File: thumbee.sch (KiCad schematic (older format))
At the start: 1 part, among them U1 msc313e

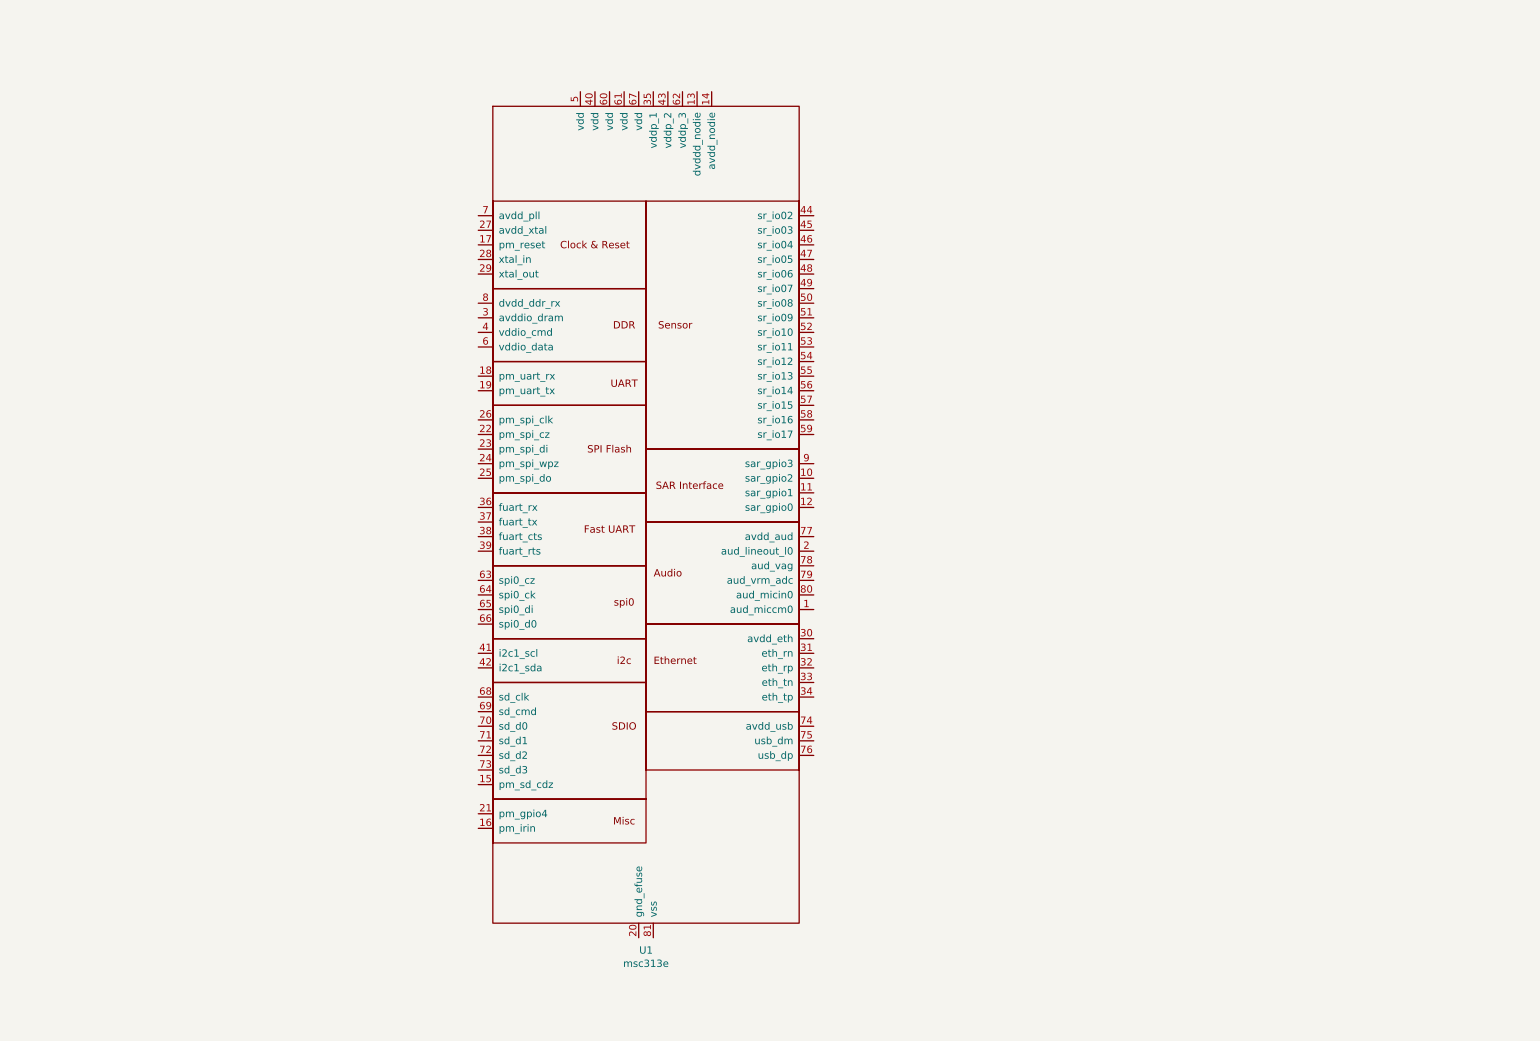
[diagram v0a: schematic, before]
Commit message: Add remaining required components. Clean up schematic a bit.
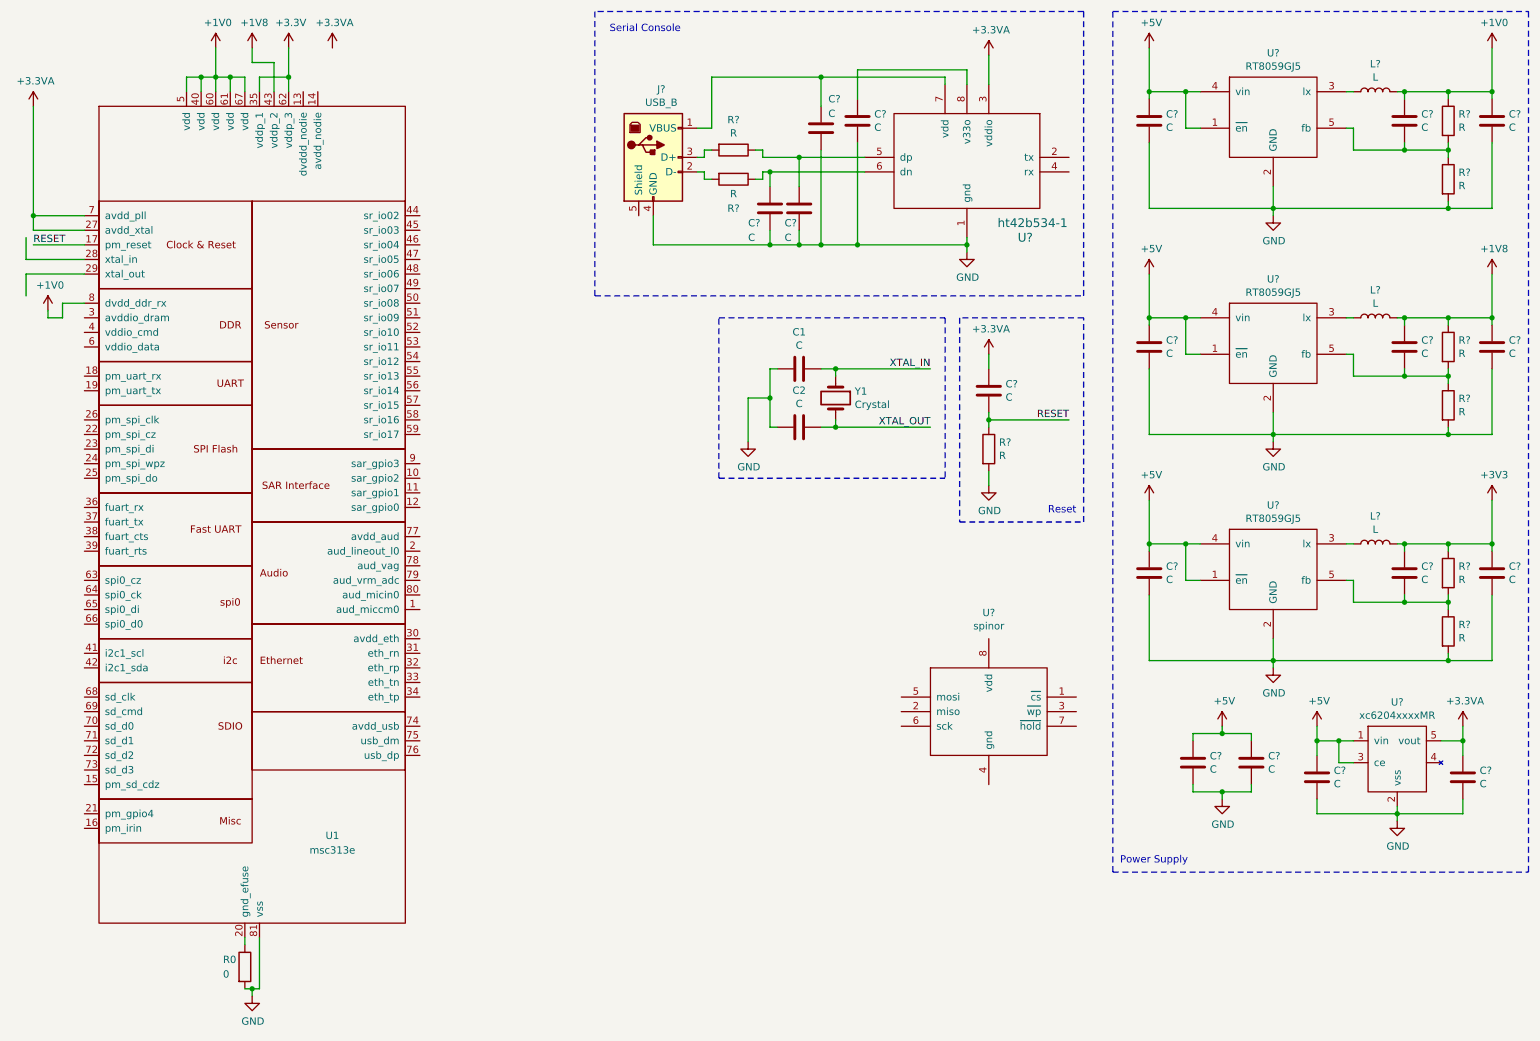
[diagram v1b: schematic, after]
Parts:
- added C1, C2, C? (x18): C, symbol Device:C
- added J?: USB_B, symbol Connector:USB_B
- added L? (x3): L, symbol Device:L
- added R0: 0, symbol Device:R
- added R? (x9): R, symbol Device:R
- added U?: ht42b534-1, symbol ht42b534-1:ht42b534-1
- added U? (x3): RT8059GJ5, symbol rt8059gj5:RT8059GJ5
- added U?: spinor, symbol spinor:spinor
- added U?: xc6204xxxxMR, symbol xc6204:xc6204xxxxMR
- added Y1: Crystal, symbol Device:Crystal
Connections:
- net RESET: now reaches U1.17 (pm_reset)
- net RESET: now also C?.2, R?.1
- net at U1.20 (gnd_efuse): now also R0.1
- net +3.3VA: now reaches U1.27 (avdd_xtal)
- net +3.3VA: now also U1.7 (avdd_pll), C?.1, C?.1, U?.3 (vddio), U?.5 (vout)
- net +3V3: now reaches U1.35 (vddp_1)
- net +3V3: now also U1.62 (vddp_3), C?.1, C?.1, L?.2, R?.1
- net +1V0: now reaches U1.40 (vdd)
- net +1V0: now also U1.5 (vdd), U1.60 (vdd), U1.61 (vdd), U1.67 (vdd), U1.8 (dvdd_ddr_rx), C?.1, C?.1, L?.2, R?.1
- net +1V8: now reaches U1.43 (vddp_2)
- net +1V8: now also C?.1, C?.1, L?.2, R?.1
- net GND: now reaches U1.81 (vss)
- net GND: now also C1.2, C2.1, C?.2, C?.2, C?.2, C?.2, C?.2, C?.2, C?.2, C?.2, C?.2, C?.2, C?.2, C?.2, C?.2, C?.2, J?.4 (GND), R0.2, R?.2, R?.2, R?.2, R?.2, U?.1 (gnd), U?.2 (GND), U?.2 (GND), U?.2 (GND), U?.2 (vss)
- new net: C?.1, R?.1, U?.5 (dp)
- new net: C?.1, R?.1, U?.6 (dn)
- new net: C?.1, J?.1 (VBUS), U?.7 (vdd)
- new net: C?.1, U?.8 (v33o)
- new net: L?.1, U?.3 (lx) (x3)
- new net: C?.2, R?.1, R?.2, U?.5 (fb) (x3)
- new net: J?.2 (D-), R?.2
- new net: J?.3 (D+), R?.2
- new net +5V: C?.1, C?.1, C?.1, C?.1, C?.1, C?.1, U?.1 (vin), U?.1 (~en), U?.1 (~en), U?.1 (~en), U?.3 (ce), U?.4 (vin), U?.4 (vin), U?.4 (vin)
- new net XTAL_IN: C1.1, Y1.1
- new net XTAL_OUT: C2.2, Y1.2
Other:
- note added: "Power Supply"
- note added: "Reset"
- note added: "Serial Console"
- moved on the sheet: U1

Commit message: Almost complete schematic
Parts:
- added C? (x6): C, symbol Device:C
- added J10, J11, J4: Conn_01x02_Male, symbol Connector:Conn_01x02_Male
- added J12: Conn_02x05_Odd_Even, symbol Connector_Generic:Conn_02x05_Odd_Even
- added J2, J3, J7, J9: Conn_01x04_Male, symbol Connector:Conn_01x04_Male
- added J5: Conn_01x07_Male, symbol Connector:Conn_01x07_Male
- added J6: Conn_01x16_Male, symbol Connector:Conn_01x16_Male
- added J8: Conn_01x05_Male, symbol Connector:Conn_01x05_Male
- added R10, R2, R3, R5, R6, R7, R8, R9, R?: R, symbol Device:R
- gave numbers to parts that had none: 12
- renumbered R0 to R1
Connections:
- net XTAL_OUT is gone; now on net xtal_out: C2.2, Y1.2
- net +1V8: now also U1.3 (avddio_dram), U1.4 (vddio_cmd), U1.6 (vddio_data), C?.1, C?.1, C?.1, R10.1, R5.1, R7.1, R8.1, R9.1, R?.1; no longer U1.43 (vddp_2)
- net +3.3VA: now also U1.14 (avdd_nodie), U1.30 (avdd_eth), U1.74 (avdd_usb), U1.77 (avdd_aud)
- net +3V3: now also U2.8 (vdd), C?.1, J12.1 (Pin_1), R6.1; no longer U1.35 (vddp_1), U1.62 (vddp_3)
- net +5V: no longer U7.1 (~en)
- net GND: now also U2.4 (gnd), C?.1, C?.2, C?.2, C?.2, C?.2, C?.2, J12.10 (Pin_10)
- net at U1.1 (aud_miccm0): now also J8.5 (Pin_5)
- net at U1.10 (sar_gpio2): now also J7.2 (Pin_2)
- net at U1.11 (sar_gpio1): now also J7.3 (Pin_3)
- net at U1.12 (sar_gpio0): now also J7.4 (Pin_4)
- net dvdd_nodie: now reaches U1.13 (dvddd_nodie)
- net dvdd_nodie: now also C?.2
- net at U1.15 (pm_sd_cdz): now also J5.7 (Pin_7)
- net console_tx: now reaches U1.18 (pm_uart_rx)
- net console_tx: now also U3.2 (tx)
- net console_rx: now reaches U1.19 (pm_uart_tx)
- net console_rx: now also U3.4 (rx)
- net at U1.2 (aud_lineout_l0): now also J8.1 (Pin_1)
- net gnd_efuse: now reaches R1.1, U1.20 (gnd_efuse)
- net at U1.21 (pm_gpio4): now also J11.1 (Pin_1)
- net spinor_cs: now reaches U1.22 (pm_spi_cz)
- net spinor_cs: now also U2.1 (~cs), J12.2 (Pin_2)
- net spinor_miso: now reaches U1.23 (pm_spi_di)
- net spinor_miso: now also U2.2 (miso), J12.5 (Pin_5)
- net spinor_wp: now reaches U1.24 (pm_spi_wpz)
- net spinor_wp: now also U2.3 (~wp), J12.4 (Pin_4)
- net spinor_mosi: now reaches U1.25 (pm_spi_do)
- net spinor_mosi: now also U2.5 (mosi), J12.3 (Pin_3)
- net spinor_clk: now reaches U1.26 (pm_spi_clk)
- net xtal_in: now reaches U1.28 (xtal_in)
- net xtal_in: now also R2.1
- net xtal_out: now reaches U1.29 (xtal_out)
- net xtal_out: now also R3.2
- net at U1.31 (eth_rn): now also J9.1 (Pin_1)
- net at U1.32 (eth_rp): now also J9.2 (Pin_2)
- net at U1.33 (eth_tn): now also J9.3 (Pin_3)
- net at U1.34 (eth_tp): now also J9.4 (Pin_4)
- net at U1.36 (fuart_rx): now also J2.1 (Pin_1)
- net at U1.37 (fuart_tx): now also J2.2 (Pin_2)
- net at U1.38 (fuart_cts): now also J2.3 (Pin_3)
- net at U1.39 (fuart_rts): now also J2.4 (Pin_4)
- net at U1.41 (i2c1_scl): now also J4.1 (Pin_1)
- net at U1.42 (i2c1_sda): now also J4.2 (Pin_2)
- net at U1.44 (sr_io02): now also J6.1 (Pin_1)
- net at U1.45 (sr_io03): now also J6.2 (Pin_2)
- net at U1.46 (sr_io04): now also J6.3 (Pin_3)
- net at U1.47 (sr_io05): now also J6.4 (Pin_4)
- net at U1.48 (sr_io06): now also J6.5 (Pin_5)
- net at U1.49 (sr_io07): now also J6.6 (Pin_6)
- net at U1.50 (sr_io08): now also J6.7 (Pin_7)
- net at U1.51 (sr_io09): now also J6.8 (Pin_8)
- net at U1.52 (sr_io10): now also J6.9 (Pin_9)
- net at U1.53 (sr_io11): now also J6.10 (Pin_10)
- net at U1.54 (sr_io12): now also J6.11 (Pin_11)
- net at U1.55 (sr_io13): now also J6.12 (Pin_12)
- net at U1.56 (sr_io14): now also J6.13 (Pin_13)
- net at U1.57 (sr_io15): now also J6.14 (Pin_14)
- net at U1.58 (sr_io16): now also J6.15 (Pin_15)
- net at U1.59 (sr_io17): now also J6.16 (Pin_16)
- net at U1.63 (spi0_cz): now also J3.1 (Pin_1)
- net at U1.64 (spi0_ck): now also J3.2 (Pin_2)
- net at U1.65 (spi0_di): now also J3.3 (Pin_3)
- net at U1.66 (spi0_d0): now also J3.4 (Pin_4)
- net at U1.68 (sd_clk): now also J5.1 (Pin_1)
- net at U1.69 (sd_cmd): now also J5.2 (Pin_2)
- net at U1.70 (sd_d0): now also J5.3 (Pin_3)
- net at U1.71 (sd_d1): now also J5.4 (Pin_4)
- net at U1.72 (sd_d2): now also J5.5 (Pin_5)
- net at U1.73 (sd_d3): now also J5.6 (Pin_6)
- net at U1.75 (usb_dm): now also J10.1 (Pin_1)
- net at U1.76 (usb_dp): now also J10.2 (Pin_2)
- net at U1.78 (aud_vag): now also J8.2 (Pin_2)
- net at U1.79 (aud_vrm_adc): now also J8.3 (Pin_3)
- net at U1.80 (aud_micin0): now also J8.4 (Pin_4)
- net at U1.9 (sar_gpio3): now also J7.1 (Pin_1)
- net spinor_sck: now reaches U2.6 (sck)
- net spinor_sck: now also J12.7 (Pin_7)
- net spinor_hold: now reaches U2.7 (~hold)
- net spinor_hold: now also J12.9 (Pin_9)
- net RESET renamed reset
- net reset: now also J12.8 (Pin_8)
- net XTAL_IN: no longer names the net of C1.1, Y1.1
- net XTAL_IN: now also R2.2, R3.1
- new net: C?.1, R?.2, U7.1 (~en)
- new net vddp1: R5.2, R6.2, U1.35 (vddp_1)
- new net vddp2: R7.2, R8.2, U1.43 (vddp_2)
- new net vddp3: R10.2, R9.2, U1.62 (vddp_3)
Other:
- note added: "Clock"
- note added: "IO Voltage jumpers"
- note added: "SPI Flash and programming header"
- note added: "efuse prog enable"
- moved on the sheet: C1, C2, C3, C?, J1, R1, R3, R?, U1, U2, U3, Y1
